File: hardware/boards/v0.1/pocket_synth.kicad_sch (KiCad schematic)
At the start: 6 parts

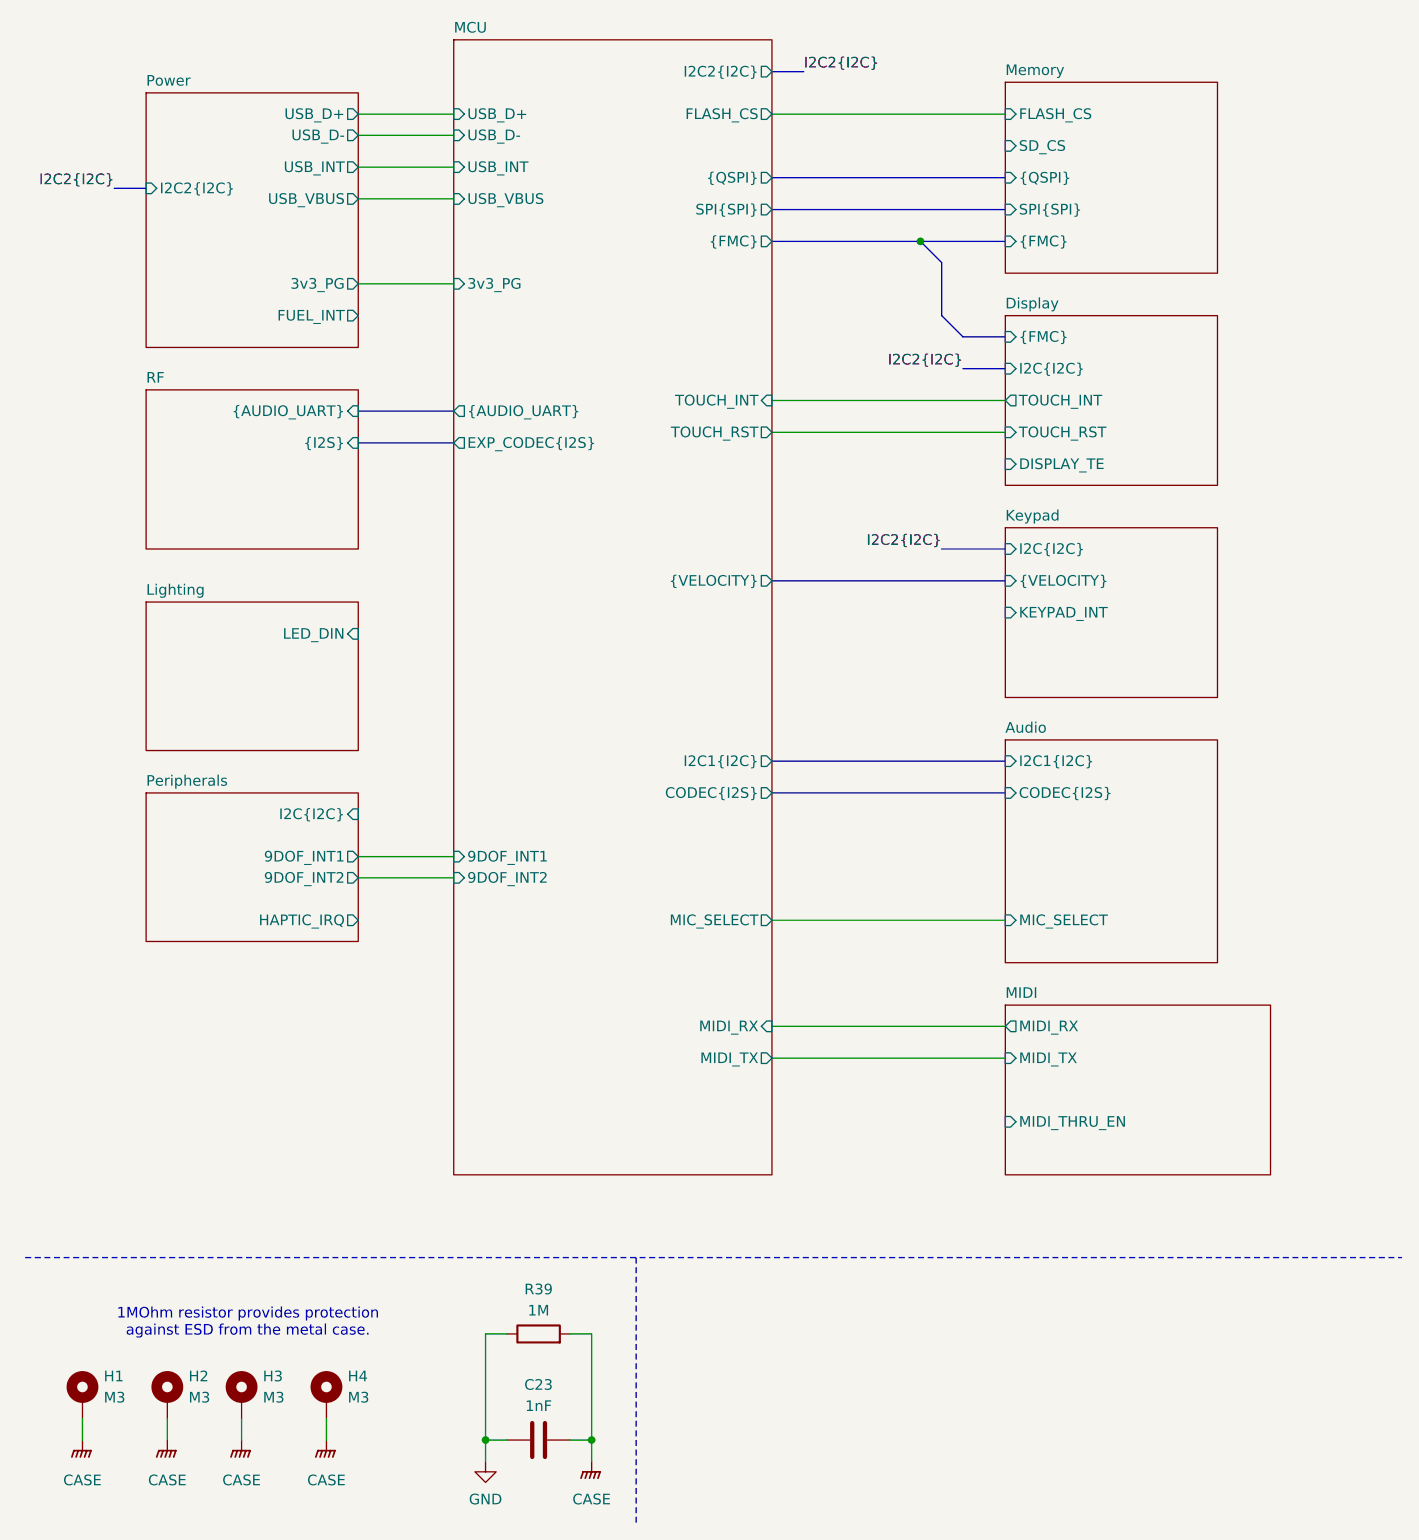
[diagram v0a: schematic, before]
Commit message: fix: DRC drill clearance errors
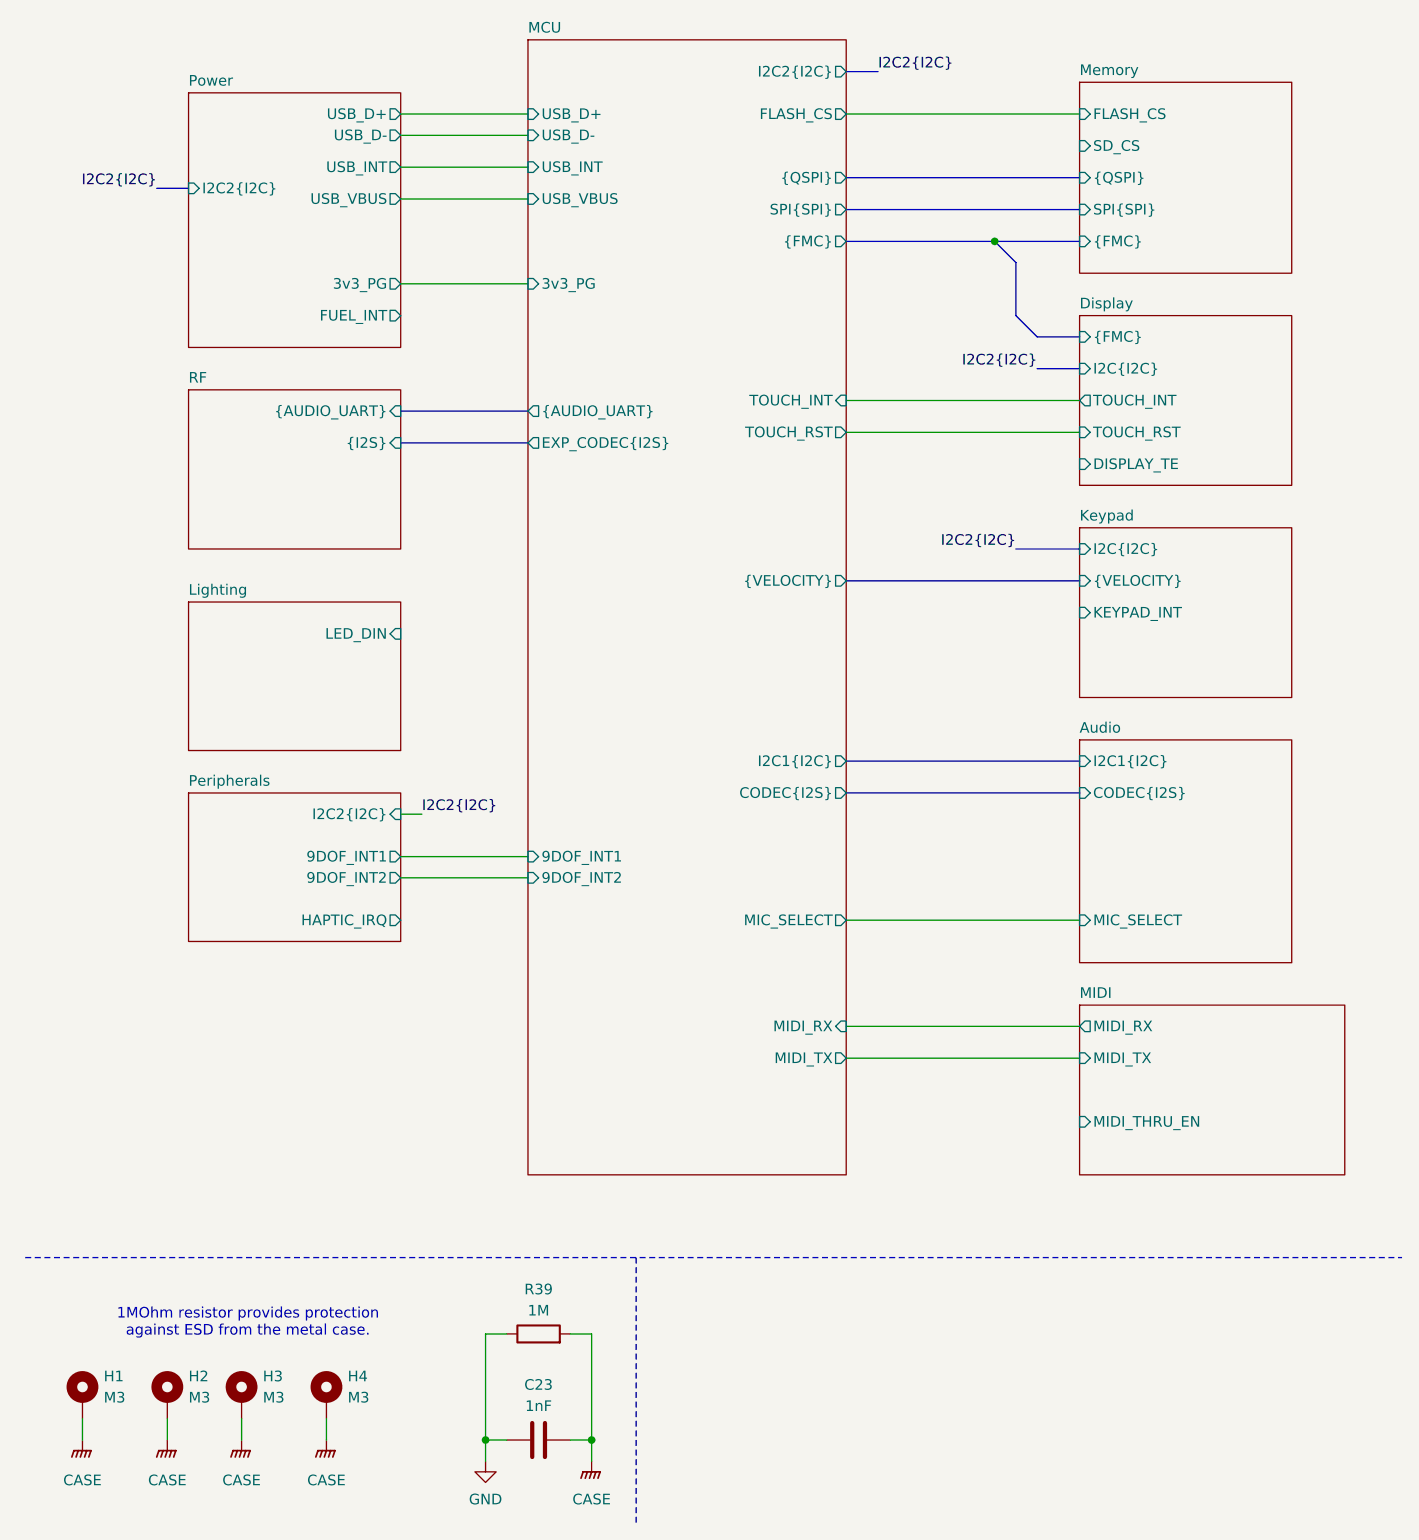
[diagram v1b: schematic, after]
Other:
- sheet Peripherals ports: added I2C2{I2C}; removed I2C{I2C}

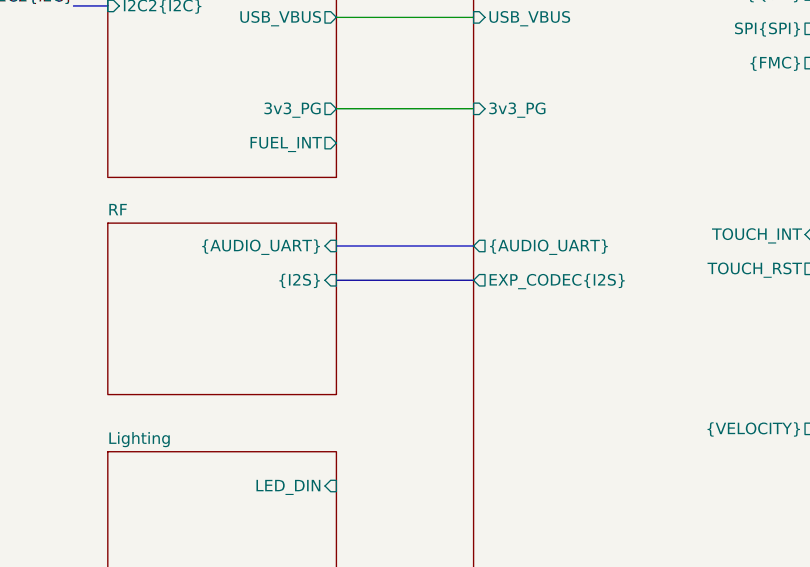
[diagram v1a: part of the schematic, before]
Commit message: feat: various routing and organization
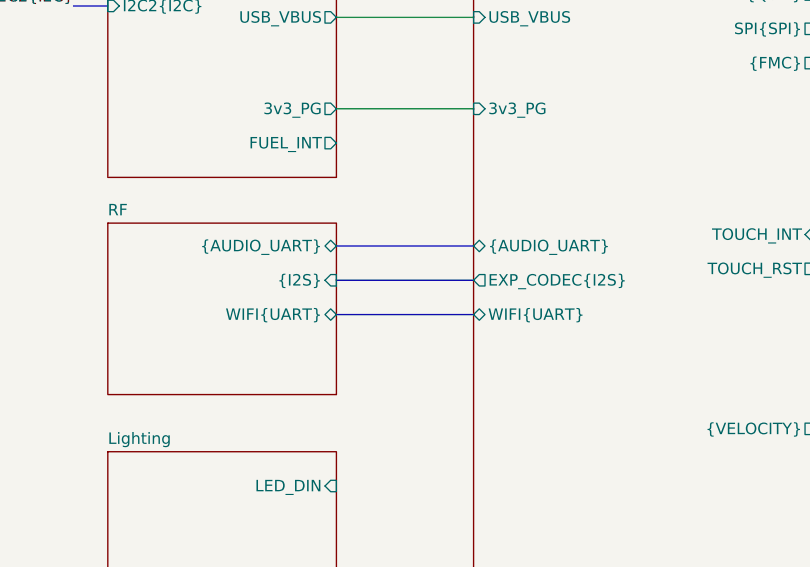
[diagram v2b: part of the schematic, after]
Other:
- sheet MCU ports: added WIFI{UART}; removed none
- sheet RF ports: added WIFI{UART}; removed none
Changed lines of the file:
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@@
+		)
+	)
+	(bus
+		(pts
+			(xy 57.15 72.39) (xy 72.39 72.39)
+		)
+		(stroke
+			(width 0)
+			(type default)
 		)
 	)
@@
 			)
 		)
-		(pin "{AUDIO_UART}" output
+		(pin "{AUDIO_UART}" bidirectional
 			(at 72.39 64.77 180)
 			(effects
@@
 				)
 				(justify right)
+			)
+		)
+		(pin "WIFI{UART}" bidirectional
+			(at 72.39 72.39 180)
+			(effects
+				(font
+					(size 1.27 1.27)
+				)
+				(justify left)
 			)
 		)
@@
 			)
 		)
-		(pin "{AUDIO_UART}" input
+		(pin "{AUDIO_UART}" bidirectional
 			(at 57.15 64.77 0)
 			(effects
 				(font
+					(size 1.27 1.27)
+				)
+				(justify right)
+			)
+		)
+		(pin "WIFI{UART}" bidirectional
+			(at 57.15 72.39 0)
+			(effects
+				(font

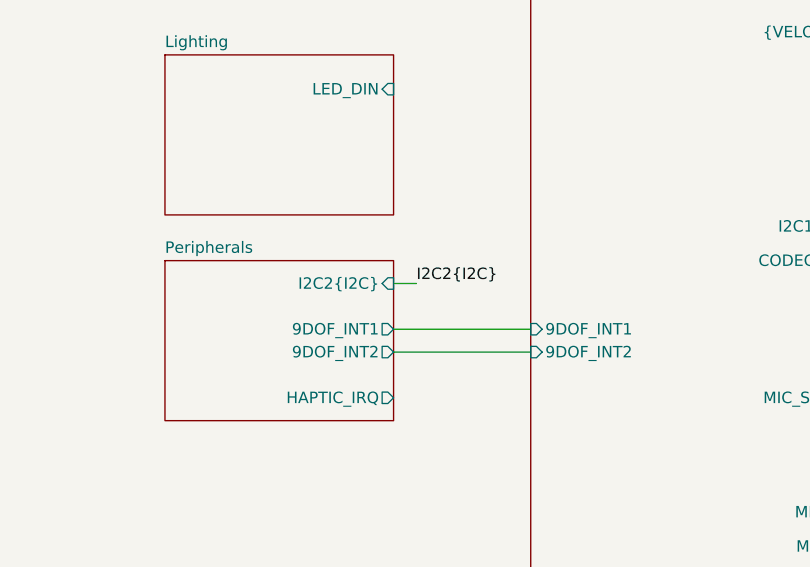
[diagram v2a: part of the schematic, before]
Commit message: feat: add missing power button controller
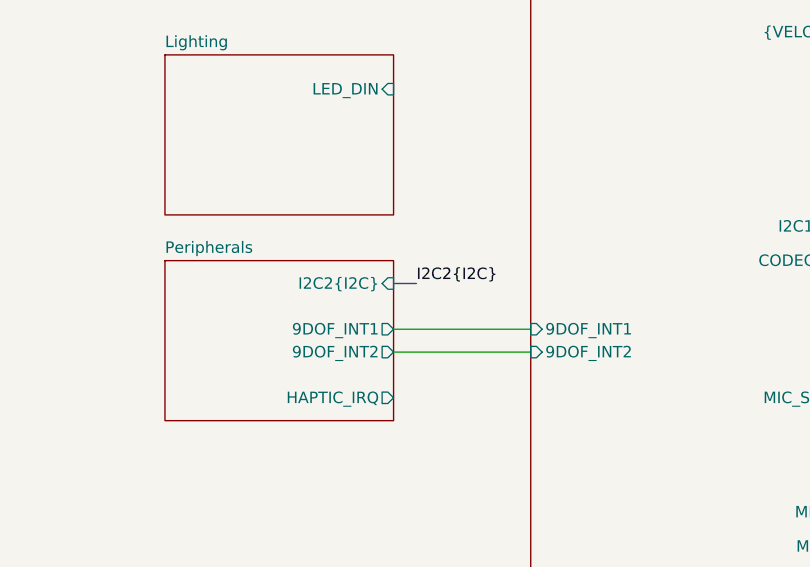
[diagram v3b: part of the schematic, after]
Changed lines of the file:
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@@
-		)
-	)
-	(wire
-		(pts
-			(xy 57.15 113.03) (xy 59.69 113.03)
-		)
-		(stroke
-			(width 0)
-			(type default)
 		)
 	)
@@
 		)
 		(stroke
+			(width 0)
+			(type default)
+		)
+	)
+	(bus
+		(pts
+			(xy 57.15 113.03) (xy 59.69 113.03)
+		)
+		(stroke

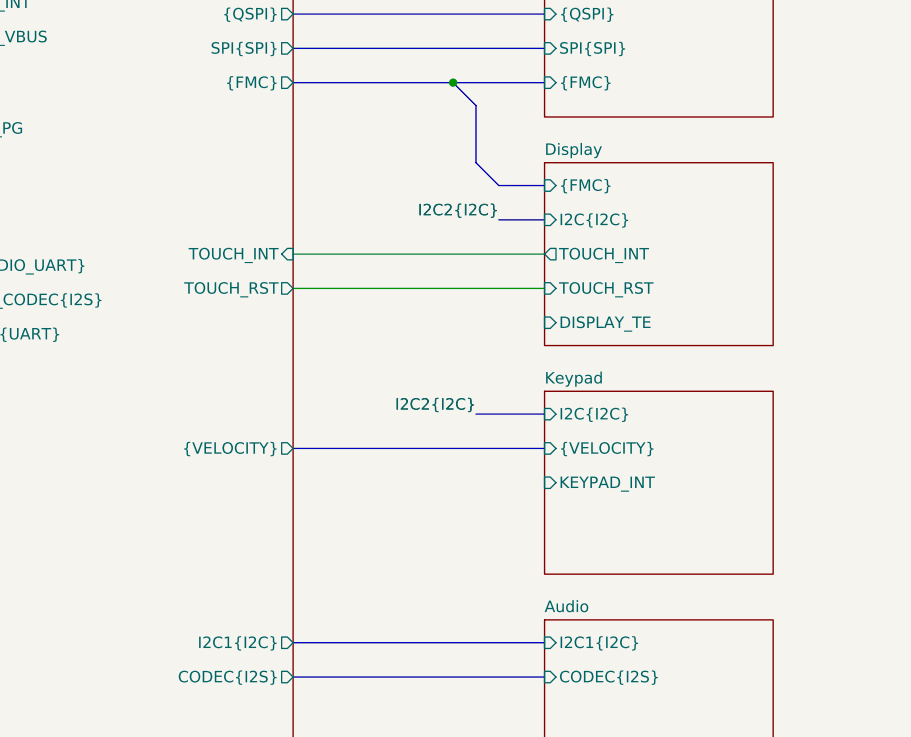
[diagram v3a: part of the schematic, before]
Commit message: feat: add touch screen connector, input I2C bus
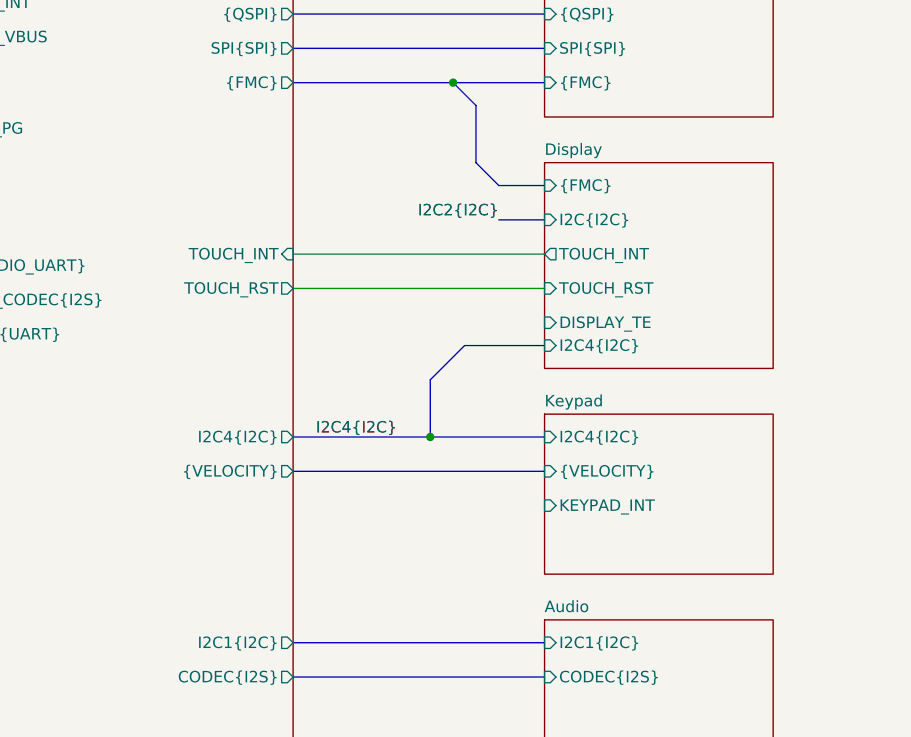
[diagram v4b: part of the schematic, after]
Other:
- sheet Display ports: added I2C4{I2C}; removed none
- sheet Keypad ports: added I2C4{I2C}; removed I2C{I2C}
- sheet MCU ports: added I2C4{I2C}; removed none
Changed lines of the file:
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@@
 		(color 0 0 0 0)
 	)
+	(junction
+		(at 125.73 83.82)
+		(diameter 0)
+		(color 0 0 0 0)
+	)
 	(wire
 		(pts
@@
 	(bus
 		(pts
+			(xy 129.54 73.66) (xy 125.73 77.47)
+		)
+		(stroke
+			(width 0)
+			(type default)
+		)
+	)
+	(bus
+		(pts
 			(xy 133.35 55.88) (xy 138.43 55.88)
 		)
@@
 	(bus
 		(pts
+			(xy 138.43 73.66) (xy 129.54 73.66)
+		)
+		(stroke
+			(width 0)
+			(type default)
+		)
+	)
+	(bus
+		(pts
 			(xy 110.49 36.83) (xy 138.43 36.83)
 		)
@@
 		(pts
 			(xy 69.85 187.96) (xy 67.31 187.96)
+		)
+		(stroke
+			(width 0)
+			(type default)
+		)
+	)
+	(bus
+		(pts
+			(xy 110.49 83.82) (xy 125.73 83.82)
 		)
 		(stroke
@@
 	(bus
 		(pts
-			(xy 110.49 85.09) (xy 138.43 85.09)
+			(xy 110.49 87.63) (xy 138.43 87.63)
 		)
 		(stroke
@@
 		)
 	)
+	(wire
+		(pts
+			(xy 110.49 142.24) (xy 138.43 142.24)
+		)
+		(stroke
+			(width 0)
+			(type default)
+		)
+	)
+	(wire
+		(pts
+			(xy 77.47 175.26) (xy 80.01 175.26)
+		)
+		(stroke
+			(width 0)
+			(type default)
+		)
+	)
+	(wire
+		(pts
+			(xy 67.31 175.26) (xy 67.31 187.96)
+		)
+		(stroke
+			(width 0)
+			(type default)
+		)
+	)
 	(bus
 		(pts
-			(xy 138.43 81.28) (xy 130.81 81.28)
+			(xy 110.49 110.49) (xy 138.43 110.49)
+		)
+		(stroke
+			(width 0)
+			(type default)
+		)
+	)
+	(bus
+		(pts
+			(xy 125.73 83.82) (xy 138.43 83.82)
 		)
 		(stroke
@@
 	(wire
 		(pts
-			(xy 110.49 142.24) (xy 138.43 142.24)
+			(xy 48.26 185.42) (xy 48.26 187.96)
+		)
+		(stroke
+			(width 0)
+			(type default)
+		)
+	)
+	(bus
+		(pts
+			(xy 27.94 38.1) (xy 31.75 38.1)
 		)
 		(stroke
@@
 	(wire
 		(pts
-			(xy 77.47 175.26) (xy 80.01 175.26)
+			(xy 57.15 120.65) (xy 72.39 120.65)
 		)
 		(stroke
@@
 	(wire
 		(pts
-			(xy 67.31 175.26) (xy 67.31 187.96)
+			(xy 80.01 175.26) (xy 80.01 187.96)
 		)
 		(stroke
@@
 	(bus
 		(pts
-			(xy 110.49 110.49) (xy 138.43 110.49)
-		)
-		(stroke
-			(width 0)
-			(type default)
-		)
-	)
-	(wire
-		(pts
-			(xy 48.26 185.42) (xy 48.26 187.96)
-		)
-		(stroke
-			(width 0)
-			(type default)
-		)
-	)
-	(bus
-		(pts
-			(xy 27.94 38.1) (xy 31.75 38.1)
-		)
-		(stroke
-			(width 0)
-			(type default)
-		)
-	)
-	(wire
-		(pts
-			(xy 57.15 120.65) (xy 72.39 120.65)
-		)
-		(stroke
-			(width 0)
-			(type default)
-		)
-	)
-	(wire
-		(pts
-			(xy 80.01 175.26) (xy 80.01 187.96)
+			(xy 125.73 77.47) (xy 125.73 83.82)
 		)
 		(stroke
@@
 	)
 	(label "I2C2{I2C}"
-		(at 130.81 81.28 180)
-		(effects
-			(font
-				(size 1.27 1.27)
-				(thickness 0.1588)
-			)
-			(justify right bottom)
-		)
-	)
-	(label "I2C2{I2C}"
 		(at 133.35 59.69 180)
 		(effects
@@
 			)
 			(justify right bottom)
+		)
+	)
+	(label "I2C4{I2C}"
+		(at 113.03 83.82 0)
+		(effects
+			(font
+				(size 1.27 1.27)
+			)
+			(justify left bottom)
 		)
 	)
@@
 		)
 		(pin "{VELOCITY}" output
-			(at 110.49 85.09 0)
+			(at 110.49 87.63 0)
 			(effects
 				(font
@@
 				)
 				(justify left)
+			)
+		)
+		(pin "I2C4{I2C}" output
+			(at 110.49 83.82 0)
+			(effects
+				(font
+					(size 1.27 1.27)
+				)
+				(justify right)
 			)
 		)
@@
 	)
 	(sheet
-		(at 138.43 78.74)
-		(size 25.4 20.32)
+		(at 138.43 81.28)
+		(size 25.4 17.78)
 		(exclude_from_sim no)
 		(in_bom yes)
@@
 		)
 		(property "Sheetname" "Keypad"
-			(at 138.43 78.0284 0)
+			(at 138.43 80.5684 0)
 			(effects
 				(font
@@
 		)
 		(pin "KEYPAD_INT" input
-			(at 138.43 88.9 180)
-			(effects
-				(font
-					(size 1.27 1.27)
-				)
-				(justify left)
-			)
-		)
-		(pin "I2C{I2C}" input
-			(at 138.43 81.28 180)
+			(at 138.43 91.44 180)
 			(effects
 				(font
@@
 		)
 		(pin "{VELOCITY}" input
-			(at 138.43 85.09 180)
+			(at 138.43 87.63 180)
+			(effects
+				(font
+					(size 1.27 1.27)
+				)
+				(justify left)
+			)
+		)
+		(pin "I2C4{I2C}" input
+			(at 138.43 83.82 180)
 			(effects
 				(font
@@
 	(sheet
 		(at 138.43 53.34)
-		(size 25.4 20.32)
+		(size 25.4 22.86)
 		(exclude_from_sim no)
 		(in_bom yes)
@@
 		)
 		(property "Sheetfile" "display.kicad_sch"
-			(at 138.43 74.2446 0)
+			(at 138.43 76.7846 0)
 			(effects
 				(font
@@
 			(effects
 				(font
+					(size 1.27 1.27)
+				)
+				(justify left)
+			)
+		)
+		(pin "I2C4{I2C}" input
+			(at 138.43 73.66 180)
+			(effects
+				(font
